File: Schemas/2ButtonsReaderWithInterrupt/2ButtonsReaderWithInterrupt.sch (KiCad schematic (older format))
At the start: 17 parts, among them J1 PWR, J2 Btn out, J3 Btn in, J4 Interrupt, U1 LM393

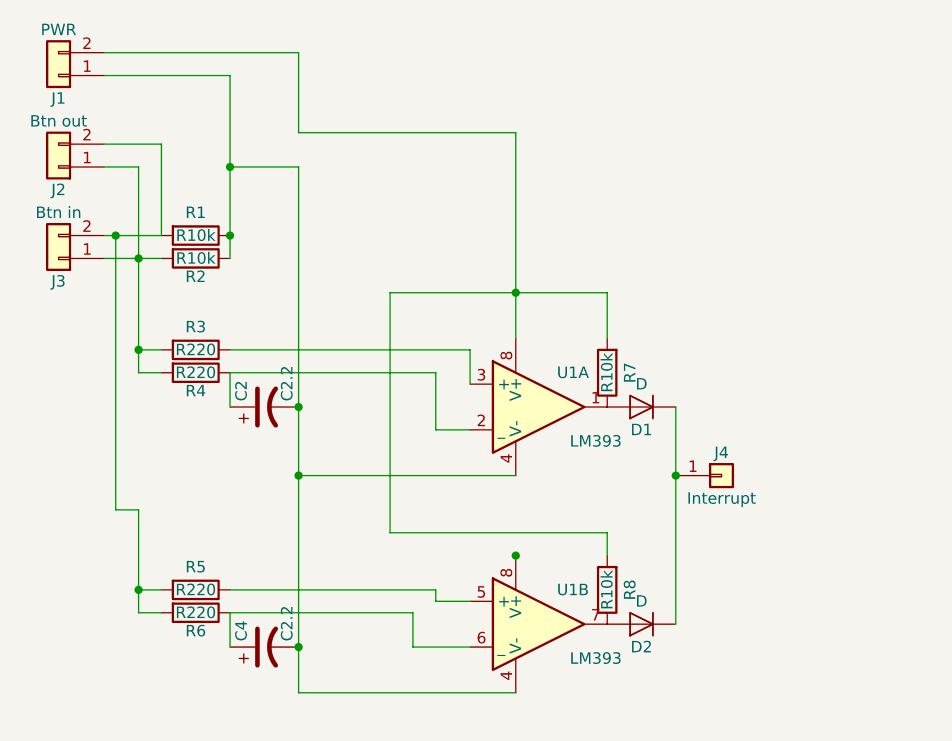
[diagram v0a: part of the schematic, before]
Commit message: Add a pull down resistor
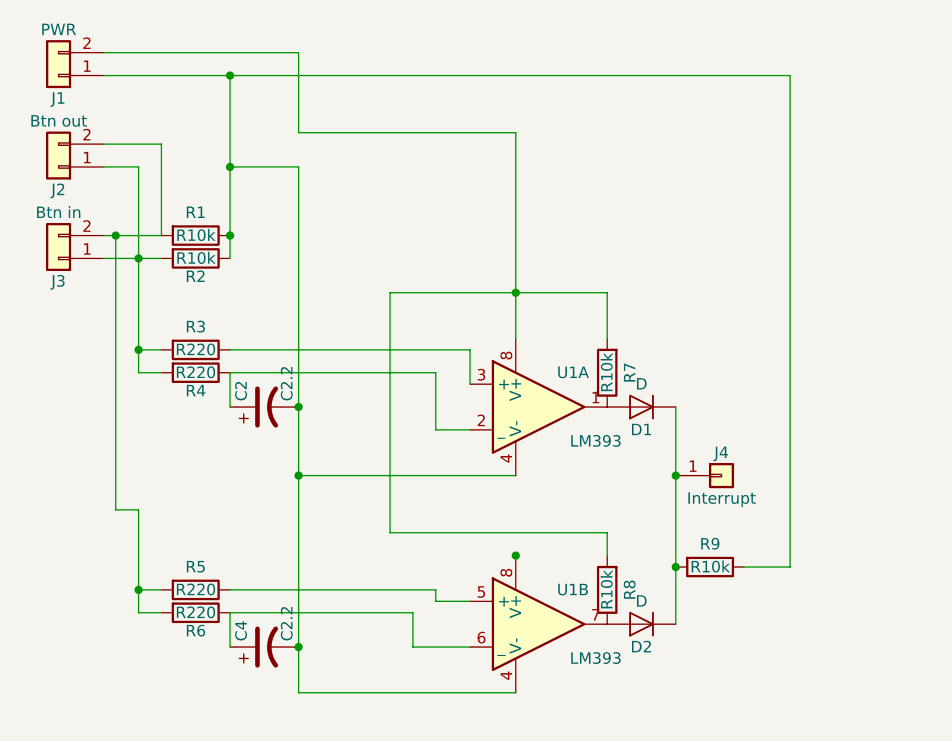
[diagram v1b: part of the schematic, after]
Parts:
- added R9: R10k, Resistors_THT:R_Box_L13.0mm_W4.0mm_P9.00mm, symbol R
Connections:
- net at C2.2, C4.2, J1.1 (Pin_1)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: now also R9.1
- net at D1.1 (K), D2.1 (K), J4.1 (Pin_1): now also R9.2
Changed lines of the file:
@@
 	2400 2000 2400 2800
 Wire Wire Line
-	2400 2000 1850 2000
+	1850 2000 4850 2000
 Wire Wire Line
 	2700 1900 1850 1900
-Wire Wire Line
-	4350 3450 4350 4400
 Connection ~ 4350 3750
 Wire Wire Line
@@
 Wire Wire Line
 	3100 4000 3100 2950
+$Comp
+L R R9
+U 1 1 59DE55FE
+P 4500 4150
+F 0 "R9" V 4400 4150 50  0000 C CNN
+F 1 "R10k" V 4500 4150 50  0000 C CNN
+F 2 "Resistors_THT:R_Box_L13.0mm_W4.0mm_P9.00mm" V 4430 4150 50  0001 C CNN
+F 3 "" H 4500 4150 50  0001 C CNN
+	1    4500 4150
+	0    1    1    0
+$EndComp
+Wire Wire Line
+	4650 4150 4850 4150
+Wire Wire Line
+	4850 4150 4850 2000
+Connection ~ 2400 2000
+Wire Wire Line
+	4350 3450 4350 4400
+Connection ~ 4350 4150
 $EndSCHEMATC

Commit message: Change 2ButtonsReaderWithInterrupt schema
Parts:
- added C1, C3: C2.2, Capacitors_THT:CP_Radial_D5.0mm_P2.00mm, symbol CP1
- C2, C4: value C2.2 -> C4.7
- J1: footprint Socket_Strips:Socket_Strip_Straight_1x02_Pitch2.54mm -> Socket_Strips:Socket_Strip_Straight_1x04_Pitch2.54mm; symbol Conn_01x02 -> Conn_01x04
- J2: value Btn out -> Btn A
- J3: value Btn in -> Btn B
- R9: value R10k -> R100k
- renumbered U1 to U2
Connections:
- net at J2.1 (Pin_1), R3.2, R4.2: now also J2.2 (Pin_2), R1.2; no longer J3.1 (Pin_1), R2.2
- net at J3.2 (Pin_2), R5.2, R6.2: now also J3.1 (Pin_1), R2.2; no longer J2.2 (Pin_2), R1.2
- net at C2.2, C4.2, J1.1 (Pin_1)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: now also C1.2, C3.2
- net at R3.1, U1.3 (+): now also C1.1
- net at R5.1: now also U2.3 (+), C3.1; no longer U2.5 (+)
- net at C4.1, R6.1: now also U2.2 (_); no longer U2.6 (_)
- net at J1.2 (Pin_2), R7.2, R8.2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: now also J1.3 (Pin_3), J1.4 (Pin_4), U2.8 (V+)
- net at D2.2 (A), R8.1: now also U2.1; no longer U2.7
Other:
- moved on the sheet: J3, R1, R2
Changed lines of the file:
@@
 L Conn_01x02 J3
 U 1 1 59CFE8EF
-P 1650 2800
-F 0 "J3" H 1650 2900 50  0000 C CNN
-F 1 "Btn in" H 1650 2600 50  0000 C CNN
-F 2 "Socket_Strips:Socket_Strip_Straight_1x02_Pitch2.54mm" H 1650 2800 50  0001 C CNN
-F 3 "" H 1650 2800 50  0001 C CNN
-	1    1650 2800
+P 1650 3850
+F 0 "J3" H 1650 3950 50  0000 C CNN
+F 1 "Btn B" H 1650 3650 50  0000 C CNN
+F 2 "Socket_Strips:Socket_Strip_Straight_1x02_Pitch2.54mm" H 1650 3850 50  0001 C CNN
+F 3 "" H 1650 3850 50  0001 C CNN
+	1    1650 3850
 	-1   0    0    1
 $EndComp
@@
 P 1650 2400
 F 0 "J2" H 1650 2500 50  0000 C CNN
-F 1 "Btn out" H 1650 2200 50  0000 C CNN
+F 1 "Btn A" H 1650 2200 50  0000 C CNN
 F 2 "Socket_Strips:Socket_Strip_Straight_1x02_Pitch2.54mm" H 1650 2400 50  0001 C CNN
 F 3 "" H 1650 2400 50  0001 C CNN
@@
 L R R1
 U 1 1 59CFEA94
-P 2250 2700
-F 0 "R1" V 2150 2700 50  0000 C CNN
-F 1 "R10k" V 2250 2700 50  0000 C CNN
-F 2 "Resistors_THT:R_Box_L13.0mm_W4.0mm_P9.00mm" V 2180 2700 50  0001 C CNN
-F 3 "" H 2250 2700 50  0001 C CNN
-	1    2250 2700
+P 2250 2300
+F 0 "R1" V 2150 2300 50  0000 C CNN
+F 1 "R10k" V 2250 2300 50  0000 C CNN
+F 2 "Resistors_THT:R_Box_L13.0mm_W4.0mm_P9.00mm" V 2180 2300 50  0001 C CNN
+F 3 "" H 2250 2300 50  0001 C CNN
+	1    2250 2300
 	0    1    1    0
 $EndComp
@@
 L R R2
 U 1 1 59CFEADA
-P 2250 2800
-F 0 "R2" V 2330 2800 50  0000 C CNN
-F 1 "R10k" V 2250 2800 50  0000 C CNN
-F 2 "Resistors_THT:R_Box_L13.0mm_W4.0mm_P9.00mm" V 2180 2800 50  0001 C CNN
-F 3 "" H 2250 2800 50  0001 C CNN
-	1    2250 2800
+P 2150 3750
+F 0 "R2" V 2250 3750 50  0000 C CNN
+F 1 "R10k" V 2150 3750 50  0000 C CNN
+F 2 "Resistors_THT:R_Box_L13.0mm_W4.0mm_P9.00mm" V 2080 3750 50  0001 C CNN
+F 3 "" H 2150 3750 50  0001 C CNN
+	1    2150 3750
 	0    1    1    0
 $EndComp
@@
 P 2550 3450
 F 0 "C2" H 2575 3550 50  0000 L CNN
-F 1 "C2.2" H 2575 3350 50  0000 L CNN
+F 1 "C4.7" H 2575 3350 50  0000 L CNN
 F 2 "Capacitors_THT:CP_Radial_D5.0mm_P2.00mm" H 2550 3450 50  0001 C CNN
 F 3 "" H 2550 3450 50  0001 C CNN
@@
 P 2550 4500
 F 0 "C4" H 2575 4600 50  0000 L CNN
-F 1 "C2.2" H 2575 4400 50  0000 L CNN
+F 1 "C4.7" H 2575 4400 50  0000 L CNN
 F 2 "Capacitors_THT:CP_Radial_D5.0mm_P2.00mm" H 2550 4500 50  0001 C CNN
 F 3 "" H 2550 4500 50  0001 C CNN
@@
 $EndComp
 $Comp
-L Conn_01x02 J1
+L Conn_01x04 J1
 U 1 1 59D0048D
-P 1650 2000
+P 1650 1900
 F 0 "J1" H 1650 2100 50  0000 C CNN
-F 1 "PWR" H 1650 1800 50  0000 C CNN
-F 2 "Socket_Strips:Socket_Strip_Straight_1x02_Pitch2.54mm" H 1650 2000 50  0001 C CNN
-F 3 "" H 1650 2000 50  0001 C CNN
-	1    1650 2000
+F 1 "PWR" H 1650 1600 50  0000 C CNN
+F 2 "Socket_Strips:Socket_Strip_Straight_1x04_Pitch2.54mm" H 1650 1900 50  0001 C CNN
+F 3 "" H 1650 1900 50  0001 C CNN
+	1    1650 1900
 	-1   0    0    1
 $EndComp
@@
 U 1 1 59D04D9B
 P 3750 3450
-F 0 "U1" H 3900 3600 50  0000 C CNN
-F 1 "LM393" H 4000 3300 50  0000 C CNN
+F 0 "U1" H 3800 3650 50  0000 C CNN
+F 1 "LM393" H 3850 3250 50  0000 C CNN
 F 2 "Housings_DIP:DIP-8_W7.62mm" H 3750 3450 50  0001 C CNN
 F 3 "" H 3750 3450 50  0001 C CNN
@@
 	1    0    0    -1
 $EndComp
-Wire Wire Line
-	1850 2700 2100 2700
-Wire Wire Line
-	1850 2800 2100 2800
-Connection ~ 2400 2700
-Wire Wire Line
-	2100 2700 2100 2300
-Wire Wire Line
-	2100 2300 1850 2300
-Wire Wire Line
-	1850 2400 2000 2400
-Wire Wire Line
-	2000 2400 2000 3300
-Connection ~ 2000 2800
-Wire Wire Line
-	2000 3300 2100 3300
-Wire Wire Line
-	2000 3200 2100 3200
-Connection ~ 2000 3200
-Wire Wire Line
-	2400 3300 2400 3450
-Wire Wire Line
-	2700 2400 2400 2400
-Connection ~ 2400 2400
-Wire Wire Line
-	2000 3900 2000 4350
-Wire Wire Line
-	2000 4350 2100 4350
-Wire Wire Line
-	2100 4250 2000 4250
-Connection ~ 2000 4250
-Wire Wire Line
-	2400 4350 2400 4500
-Wire Wire Line
-	1900 2700 1900 3900
-Wire Wire Line
-	1900 3900 2000 3900
-Connection ~ 1900 2700
-Wire Wire Line
-	2700 1900 2700 2250
-Wire Wire Line
-	2700 2250 3650 2250
-Wire Wire Line
-	2400 3200 3450 3200
-Wire Wire Line
-	2400 3300 3300 3300
-Wire Wire Line
-	2400 4250 3300 4250
-Wire Wire Line
-	2400 2000 2400 2800
-Wire Wire Line
-	1850 2000 4850 2000
-Wire Wire Line
-	2700 1900 1850 1900
-Connection ~ 4350 3750
-Wire Wire Line
-	2700 2400 2700 4700
-Connection ~ 2700 3450
-Wire Wire Line
-	3450 3200 3450 3350
-Wire Wire Line
-	3300 3300 3300 3550
-Wire Wire Line
-	3300 3550 3450 3550
-Wire Wire Line
-	3650 2250 3650 3150
-Wire Wire Line
-	4050 2950 4050 3150
-Wire Wire Line
-	3100 2950 4050 2950
-Connection ~ 3650 2950
-$Comp
-L LM393 U1
-U 2 1 59D05C02
+$Comp
+L LM393 U2
+U 1 1 59D05C02
 P 3750 4400
-F 0 "U1" H 3900 4550 50  0000 C CNN
-F 1 "LM393" H 4000 4250 50  0000 C CNN
+F 0 "U2" H 3800 4600 50  0000 C CNN
+F 1 "LM393" H 3800 4200 50  0000 C CNN
 F 2 "Housings_DIP:DIP-8_W7.62mm" H 3750 4400 50  0001 C CNN
 F 3 "" H 3750 4400 50  0001 C CNN
-	2    3750 4400
+	1    3750 4400
 	1    0    0    -1
 $EndComp
-Wire Wire Line
-	3300 4250 3300 4300
-Wire Wire Line
-	3300 4300 3450 4300
-Wire Wire Line
-	2400 4350 3200 4350
-Wire Wire Line
-	3200 4350 3200 4500
-Wire Wire Line
-	3200 4500 3450 4500
-Wire Wire Line
-	3650 3750 2700 3750
-Connection ~ 2700 3750
-Wire Wire Line
-	2700 4700 3650 4700
-Connection ~ 2700 4500
-Connection ~ 3650 4100
-Wire Wire Line
-	4050 4100 4050 4000
-Wire Wire Line
-	4050 4000 3100 4000
-Wire Wire Line
-	3100 4000 3100 2950
 $Comp
 L R R9
 U 1 1 59DE55FE
 P 4500 4150
-F 0 "R9" V 4400 4150 50  0000 C CNN
-F 1 "R10k" V 4500 4150 50  0000 C CNN
+F 0 "R9" V 4500 4150 50  0000 C CNN
+F 1 "R100k" V 4600 4150 50  0000 C CNN
 F 2 "Resistors_THT:R_Box_L13.0mm_W4.0mm_P9.00mm" V 4430 4150 50  0001 C CNN
 F 3 "" H 4500 4150 50  0001 C CNN
@@
 	0    1    1    0
 $EndComp
+$Comp
+L CP1 C3
+U 1 1 59E7BBD0
+P 2550 4100
+F 0 "C3" H 2575 4200 50  0000 L CNN
+F 1 "C2.2" H 2575 4000 50  0000 L CNN
+F 2 "Capacitors_THT:CP_Radial_D5.0mm_P2.00mm" H 2550 4100 50  0001 C CNN
+F 3 "" H 2550 4100 50  0001 C CNN
+	1    2550 4100
+	0    -1   -1   0
+$EndComp
+$Comp
+L CP1 C1
+U 1 1 59E7BD71
+P 2550 3050
+F 0 "C1" H 2575 3150 50  0000 L CNN
+F 1 "C2.2" H 2575 2950 50  0000 L CNN
+F 2 "Capacitors_THT:CP_Radial_D5.0mm_P2.00mm" H 2550 3050 50  0001 C CNN
+F 3 "" H 2550 3050 50  0001 C CNN
+	1    2550 3050
+	0    -1   -1   0
+$EndComp
+Wire Wire Line
+	2100 2300 1850 2300
+Wire Wire Line
+	1850 2400 2000 2400
+Wire Wire Line
+	2000 2300 2000 3300
+Wire Wire Line
+	2000 3300 2100 3300
+Wire Wire Line
+	2000 3200 2100 3200
+Connection ~ 2000 3200
+Wire Wire Line
+	2400 3300 2400 3450
+Wire Wire Line
+	2000 4350 2100 4350
+Wire Wire Line
+	2100 4250 2000 4250
+Connection ~ 2000 4250
+Wire Wire Line
+	2400 4350 2400 4500
+Wire Wire Line
+	2700 1700 2700 2250
+Wire Wire Line
+	2700 2250 3650 2250
+Wire Wire Line
+	2400 3200 3450 3200
+Wire Wire Line
+	2400 3300 3300 3300
+Wire Wire Line
+	2400 4250 3300 4250
+Wire Wire Line
+	1850 2000 4850 2000
+Wire Wire Line
+	2700 1900 1850 1900
+Connection ~ 4350 3750
+Wire Wire Line
+	2700 2300 2700 4700
+Connection ~ 2700 3450
+Wire Wire Line
+	3450 3200 3450 3350
+Wire Wire Line
+	3300 3300 3300 3550
+Wire Wire Line
+	3300 3550 3450 3550
+Wire Wire Line
+	3650 2250 3650 3150
+Wire Wire Line
+	4050 2950 4050 3150
+Wire Wire Line
+	3100 2950 4050 2950
+Connection ~ 3650 2950
+Wire Wire Line
+	3300 4250 3300 4300
+Wire Wire Line
+	3300 4300 3450 4300
+Wire Wire Line
+	2400 4350 3200 4350
+Wire Wire Line
+	3200 4350 3200 4500
+Wire Wire Line
+	3200 4500 3450 4500
+Wire Wire Line
+	2300 3750 3650 3750
+Connection ~ 2700 3750
+Wire Wire Line
+	2700 4700 3650 4700
+Connection ~ 2700 4500
+Wire Wire Line
+	4050 4100 4050 4000
+Wire Wire Line
+	4050 4000 3100 4000
+Wire Wire Line
+	3100 4000 3100 2950
 Wire Wire Line
 	4650 4150 4850 4150
@@
 	4350 3450 4350 4400
 Connection ~ 4350 4150
+Wire Wire Line
+	2700 1800 1850 1800
+Connection ~ 2700 1900
+Wire Wire Line
+	2700 1700 1850 1700
+Connection ~ 2700 1800
+Wire Wire Line
+	2400 3200 2400 3050
+Connection ~ 2400 3200
+Connection ~ 2400 3300
+Connection ~ 2400 4250
+Wire Wire Line
+	2400 4250 2400 4100
+Connection ~ 2700 4100
+Connection ~ 2700 3050
+Wire Wire Line
+	3650 4100 3650 4000
+Connection ~ 3650 4000
+Connection ~ 2000 2300
+Connection ~ 2000 2400
+Wire Wire Line
+	2700 2300 2400 2300
+Wire Wire Line
+	2400 2300 2400 2000
+Wire Wire Line
+	2000 3750 2000 4350
+Connection ~ 2000 3850
+Wire Wire Line
+	2000 3750 1850 3750
+Wire Wire Line
+	1850 3850 2000 3850
 $EndSCHEMATC
